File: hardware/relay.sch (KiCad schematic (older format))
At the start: 13 parts, among them J11 LOAD, K11 SRD-05VDC-SL-C, Q11 PMBT3904, U31 PC817X2CSP9F, U32 CC6902SO-10A

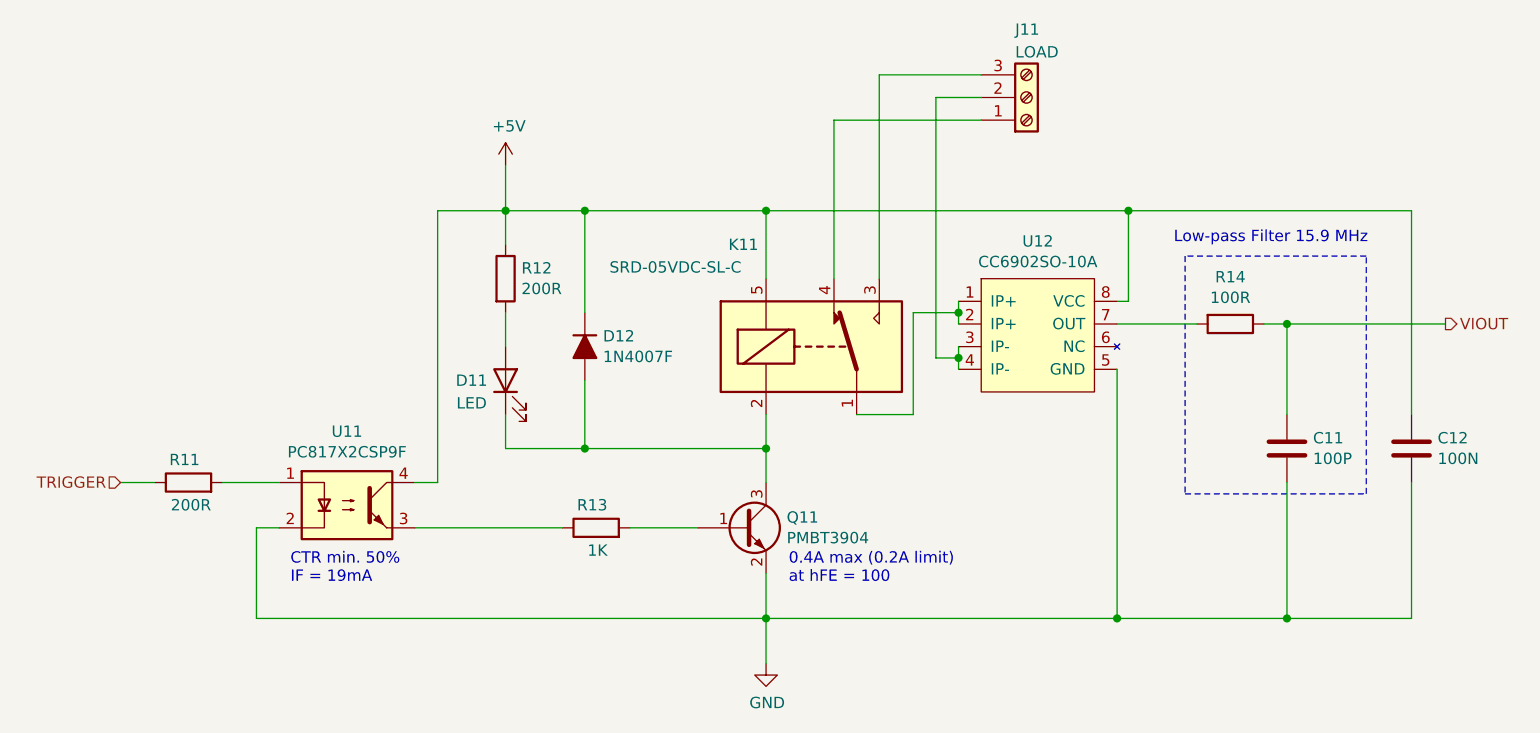
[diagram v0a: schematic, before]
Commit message: Add bjt pulldown, prepare for export
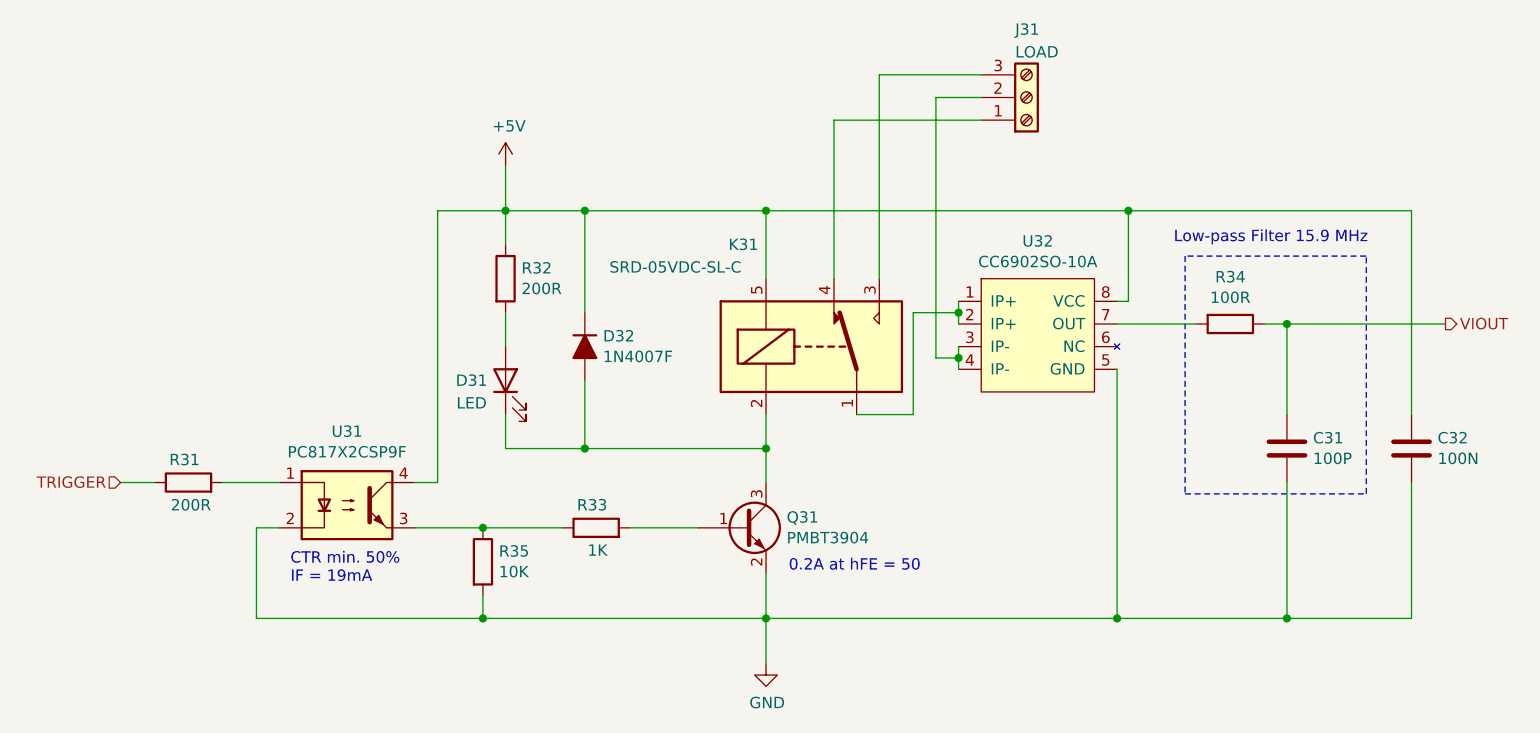
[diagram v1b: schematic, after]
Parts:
- added R15: 10K, Resistor_SMD:R_0805_2012Metric, symbol Device:R
- C11: Description / Value (none) -> CAP CER 100PF MAX. 5% MIN. 10V 0805 SMD; Distributor (none) -> Any; Distributor part # (none) -> TBD; Manufacturer (none) -> TBD; Manufacturer Part # (none) -> TBD; Package / Footprint (none) -> 0805; Type (none) -> SMD
- C12: Description / Value (none) -> CAP CER 100NF MAX. 5% MIN. 10V 0805 SMD; Distributor (none) -> Any; Distributor part # (none) -> TBD; Manufacturer (none) -> TBD; Manufacturer Part # (none) -> TBD; Package / Footprint (none) -> 0805; Type (none) -> SMD
- D11: Description / Value (none) -> LED RED 2V 0805 SMD; Distributor (none) -> LCSC; Distributor part # (none) -> C72037; Manufacturer (none) -> Everlight Elec; Manufacturer Part # (none) -> 17-21SURC/S530-A3/TR8; Package / Footprint (none) -> 0805; Type (none) -> SMD
- D12: Description / Value (none) -> DIODE 1N4007 SMAF; Distributor (none) -> LCSC; Distributor part # (none) -> C110856; Manufacturer (none) -> Shikues; Manufacturer Part # (none) -> 1N4007F; Package / Footprint (none) -> SMAF; Type (none) -> SMD
- J11: Description / Value (none) -> CONN SCREW TERMINAL PITCH-5.0MM 3 PIN 20A; Distributor (none) -> LCSC; Distributor part # (none) -> C8270; Manufacturer (none) -> Ningbo Kangnex Elec; Manufacturer Part # (none) -> WJ128V-5.0-3P; Package / Footprint (none) -> Through-Hole; Type (none) -> THT
- K11: Description / Value (none) -> RELAY 5V 10A; Distributor (none) -> LCSC; Distributor part # (none) -> C35449; Manufacturer (none) -> Ningbo Songle Relay; Manufacturer Part # (none) -> SRD-05VDC-SL-C; Package / Footprint (none) -> Through-Hole; Type (none) -> THT
- Q11: Description / Value (none) -> BJT NPN SOT-23-3; Distributor (none) -> LCSC; Distributor part # (none) -> C8667; Manufacturer (none) -> Nexperia; Manufacturer Part # (none) -> PMBT3904,215; Package / Footprint (none) -> SOT-23-3; Type (none) -> SMD
- R11, R12: Description / Value (none) -> RES 200 OHM MAX. 1% MIN. 1/8W 0805 SMD; Distributor (none) -> Any; Distributor part # (none) -> TBD; Manufacturer (none) -> TBD; Manufacturer Part # (none) -> TBD; Package / Footprint (none) -> 0805; Type (none) -> SMD
- R13: Description / Value (none) -> RES 1K OHM MAX. 1% MIN. 1/8W 0805 SMD; Distributor (none) -> Any; Distributor part # (none) -> TBD; Manufacturer (none) -> TBD; Manufacturer Part # (none) -> TBD; Package / Footprint (none) -> 0805; Type (none) -> SMD
- R14: Description / Value (none) -> RES 100 OHM MAX. 1% MIN. 1/8W 0805 SMD; Distributor (none) -> Any; Distributor part # (none) -> TBD; Manufacturer (none) -> TBD; Manufacturer Part # (none) -> TBD; Package / Footprint (none) -> 0805; Type (none) -> SMD
- U31: Description / Value (none) -> IC OPTOCOUPLER SMD-4; Distributor (none) -> LCSC; Distributor part # (none) -> C66405; Manufacturer (none) -> Sharp Microelectronics; Manufacturer Part # (none) -> PC817X2CSP9F; Package / Footprint (none) -> SMD-4; Type (none) -> SMD
- U32: Description / Value (none) -> IC CURRENT SENSOR 5V 10A SOP-8; Distributor (none) -> LCSC; Distributor part # (none) -> C350865; Manufacturer (none) -> Cross Chip; Manufacturer Part # (none) -> CC6902SO-10A; Package / Footprint (none) -> SOP-8; Type (none) -> SMD
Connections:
- net GND: now also R15.2
- net at R13.1, U31.3: now also R15.1
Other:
- note added: "0.2A at hFE = 50"
- note removed: "0.4A max (0.2A limit) \nat hFE = 100"

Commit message: rev1 final touchups
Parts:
- D12: footprint Diode_SMD:D_SMA -> CustomComponents:D_SMAF
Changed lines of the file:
@@
 F 0 "D32" V 4604 3530 50  0000 L CNN
 F 1 "1N4007F" V 4695 3530 50  0000 L CNN
-F 2 "Diode_SMD:D_SMA" H 4650 3450 50  0001 C CNN
+F 2 "CustomComponents:D_SMAF" H 4650 3450 50  0001 C CNN
 F 3 "~" H 4650 3450 50  0001 C CNN
 F 4 "DIODE 1N4007 SMAF" H 4650 3450 50  0001 C CNN "Description / Value"

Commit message: Add rev 1.1 fabrication files
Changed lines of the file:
@@
 $Descr A4 11693 8268
 encoding utf-8
-Sheet 3 5
+Sheet 2 5
 Title "Relay Subsystem"
 Date "2021-06-11"
@@
 AR Path="/60CBD77D/60D1BECF" Ref="R33"  Part="1"
 AR Path="/60CBD7BB/60D1BECF" Ref="R43"  Part="1"
-F 0 "R33" V 4800 4200 50  0000 L CNN
+F 0 "R13" V 4800 4200 50  0000 L CNN
 F 1 "1K" V 4600 4200 50  0000 L CNN
 F 2 "Resistor_SMD:R_0805_2012Metric" V 4630 4250 50  0001 C CNN
@@
 AR Path="/60CBD77D/60C4BBD2" Ref="J31"  Part="1"
 AR Path="/60CBD7BB/60C4BBD2" Ref="J41"  Part="1"
-F 0 "J31" H 6550 2050 50  0000 L CNN
+F 0 "J11" H 6550 2050 50  0000 L CNN
 F 1 "LOAD" H 6550 2150 50  0000 L CNN
 F 2 "TerminalBlock_Phoenix:TerminalBlock_Phoenix_MKDS-1,5-3_1x03_P5.00mm_Horizontal" H 6600 2350 50  0001 C CNN
@@
 AR Path="/60CBD77D/60D1BECB" Ref="K31"  Part="1"
 AR Path="/60CBD7BB/60D1BECB" Ref="K41"  Part="1"
-F 0 "K31" H 5350 3900 50  0000 C CNN
+F 0 "K11" H 5350 3900 50  0000 C CNN
 F 1 "SRD-05VDC-SL-C" H 5050 3800 50  0000 C CNN
 F 2 "Relay_THT:Relay_SPDT_SANYOU_SRD_Series_Form_C" H 6100 3400 50  0001 L CNN
@@
 AR Path="/60CBD6BF/60D1BED9" Ref="U22"  Part="1"
 AR Path="/60CBD7BB/60D1BED9" Ref="U42"  Part="1"
-F 0 "U32" H 6650 3815 50  0000 C CNN
+F 0 "U12" H 6650 3815 50  0000 C CNN
 F 1 "CC6902SO-10A" H 6650 3724 50  0000 C CNN
 F 2 "CustomComponents:CC690XSO-XA" H 6650 3100 50  0001 C CNN
@@
 AR Path="/60CBD77D/60D1BED4" Ref="C31"  Part="1"
 AR Path="/60CBD7BB/60D1BED4" Ref="C41"  Part="1"
-F 0 "C31" H 7865 3946 50  0000 L CNN
+F 0 "C11" H 7865 3946 50  0000 L CNN
 F 1 "100P" H 7865 3855 50  0000 L CNN
 F 2 "Capacitor_SMD:C_0805_2012Metric" H 7788 3750 50  0001 C CNN
@@
 AR Path="/60CBD77D/60D1BED7" Ref="R34"  Part="1"
 AR Path="/60CBD7BB/60D1BED7" Ref="R44"  Part="1"
-F 0 "R34" V 7293 3350 50  0000 C CNN
+F 0 "R14" V 7293 3350 50  0000 C CNN
 F 1 "100R" V 7384 3350 50  0000 C CNN
 F 2 "Resistor_SMD:R_0805_2012Metric" V 7430 3350 50  0001 C CNN
@@
 AR Path="/60CBD77D/60D1BED5" Ref="C32"  Part="1"
 AR Path="/60CBD7BB/60D1BED5" Ref="C42"  Part="1"
-F 0 "C32" H 8415 3946 50  0000 L CNN
+F 0 "C12" H 8415 3946 50  0000 L CNN
 F 1 "100N" H 8415 3855 50  0000 L CNN
 F 2 "Capacitor_SMD:C_0805_2012Metric" H 8338 3750 50  0001 C CNN
@@
 AR Path="/60CBD77D/60C3D896" Ref="R32"  Part="1"
 AR Path="/60CBD7BB/60C3D896" Ref="R42"  Part="1"
-F 0 "R32" H 4370 3196 50  0000 L CNN
+F 0 "R12" H 4370 3196 50  0000 L CNN
 F 1 "200R" H 4370 3105 50  0000 L CNN
 F 2 "Resistor_SMD:R_0805_2012Metric" V 4230 3150 50  0001 C CNN
@@
 AR Path="/60CBD77D/60C544FE" Ref="D32"  Part="1"
 AR Path="/60CBD7BB/60C544FE" Ref="D42"  Part="1"
-F 0 "D32" V 4604 3530 50  0000 L CNN
+F 0 "D12" V 4604 3530 50  0000 L CNN
 F 1 "1N4007F" V 4695 3530 50  0000 L CNN
 F 2 "CustomComponents:D_SMAF" H 4650 3450 50  0001 C CNN
@@
 AR Path="/60CBD77D/60C3C98C" Ref="D31"  Part="1"
 AR Path="/60CBD7BB/60C3C98C" Ref="D41"  Part="1"
-F 0 "D31" V 4300 3750 50  0000 C CNN
+F 0 "D11" V 4300 3750 50  0000 C CNN
 F 1 "LED" V 4200 3750 50  0000 C CNN
 F 2 "LED_SMD:LED_0805_2012Metric" H 4300 3600 50  0001 C CNN
@@
 AR Path="/60CBD6BF/60D16537" Ref="U21"  Part="1"
 AR Path="/60CBD7BB/60D16537" Ref="U41"  Part="1"
-F 0 "U31" H 3600 4475 50  0000 C CNN
+F 0 "U11" H 3600 4475 50  0000 C CNN
 F 1 "PC817X2CSP9F" H 3600 4384 50  0000 C CNN
 F 2 "CustomComponents:PC817X2CSP9F" H 3400 3950 50  0001 L CIN
@@
 AR Path="/60CBD77D/60C3E090" Ref="R31"  Part="1"
 AR Path="/60CBD7BB/60C3E090" Ref="R41"  Part="1"
-F 0 "R31" V 3000 4000 50  0000 L CNN
+F 0 "R11" V 3000 4000 50  0000 L CNN
 F 1 "200R" V 2800 3950 50  0000 L CNN
 F 2 "Resistor_SMD:R_0805_2012Metric" V 2830 4050 50  0001 C CNN
@@
 AR Path="/60C36AE5/60D95417" Ref="R15"  Part="1"
 AR Path="/60CBD77D/60D95417" Ref="R35"  Part="1"
-F 0 "R35" H 4270 4446 50  0000 L CNN
+F 0 "R15" H 4270 4446 50  0000 L CNN
 F 1 "10K" H 4270 4355 50  0000 L CNN
 F 2 "Resistor_SMD:R_0805_2012Metric" V 4130 4400 50  0001 C CNN
@@
 AR Path="/60CBD77D/60C3AACC" Ref="Q31"  Part="1"
 AR Path="/60CBD7BB/60C3AACC" Ref="Q41"  Part="1"
-F 0 "Q31" H 5541 4296 50  0000 L CNN
+F 0 "Q11" H 5541 4296 50  0000 L CNN
 F 1 "PMBT3904" H 5541 4205 50  0000 L CNN
 F 2 "Package_TO_SOT_SMD:SOT-23" H 5550 4350 50  0001 C CNN
